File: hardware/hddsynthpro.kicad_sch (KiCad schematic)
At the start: 0 parts

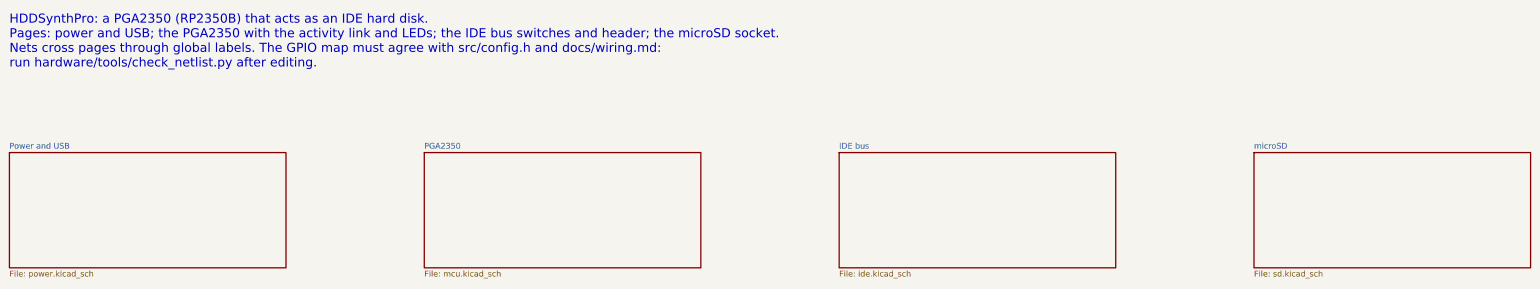
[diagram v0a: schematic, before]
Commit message: PCB rev 0.2: RP2350B on the board instead of the PGA2350 module
The PGA2350 is replaced by an RP2350B with Raspberry Pi's minimal-design
support circuit: their core regulator (polarity-marked inductor), 12 MHz
crystal, W25Q128 flash and USB 27R, with their regulator, QSPI and USB
layout copied relative to the VREG_LX pin; an AMS1117 makes 3V3. GPIO
numbers are unchanged. Supply pins each have a via under the chip.

Cheaper parts from the HDD Synth Mk5: HRO TYPE-C-31-M-12 USB-C, TS-1187A
buttons, and a generic TF PUSH microSD socket. The CB3T3245 bus switches
stay. Every symbol carries its LCSC part number, and Fabrication Toolkit
offsets where JLCPCB's footprint differs from KiCad's; jlcpcb.py applies
the same fitted corrections. check_netlist.py also checks the RP2350
support circuit. ERC and DRC are clean; parts for 5 boards about $68.50.

Co-Authored-By: Claude Opus 5.5 <noreply@anthropic.com>
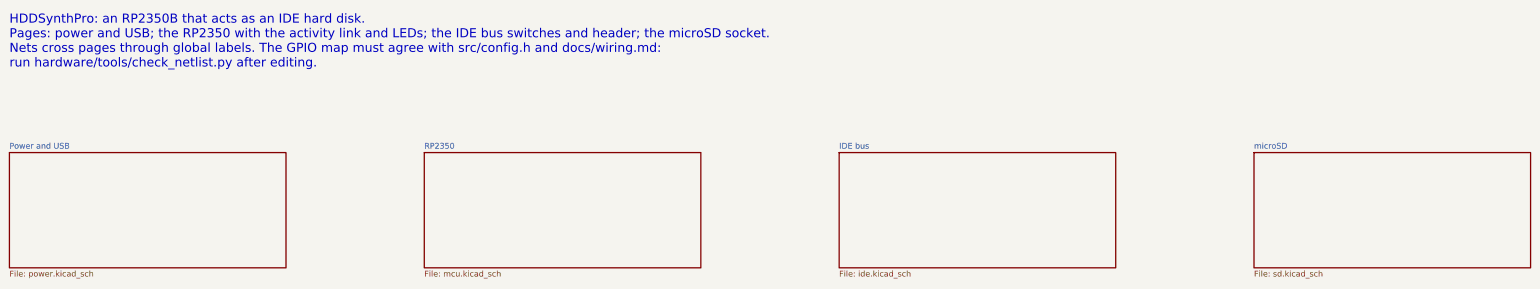
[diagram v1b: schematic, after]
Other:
- sheet PGA2350 renamed RP2350
- note added: "HDDSynthPro: an RP2350B that acts as an IDE hard disk. Pages: power and USB; the RP2350 with the activity link and LEDs; the IDE bus switches and header; the microSD socket. Nets cross pages through global labels. The GPIO map must agree with src/config.h and docs/wiring.md: run hardware/tools/check_netlist.py after editing."
- note removed: "HDDSynthPro: a PGA2350 (RP2350B) that acts as an IDE hard disk. Pages: power and USB; the PGA2350 with the activity link and LEDs; the IDE bus switches and header; the microSD socket. Nets cross pages through global labels. The GPIO map must agree with src/config.h and docs/wiring.md: run hardware/tools/check_netlist.py after editing."
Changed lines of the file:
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@@
 			(color 0 0 0 0)
 		)
-		(property "Sheetname" "PGA2350"
+		(property "Sheetname" "RP2350"
 			(at 121.92 60.2484 0)
 			(effects
@@
 		)
 	)
-	(text "HDDSynthPro: a PGA2350 (RP2350B) that acts as an IDE hard disk.\nPages: power and USB; the PGA2350 with the activity link and LEDs; the IDE bus switches and header; the microSD socket.\nNets cross pages through global labels. The GPIO map must agree with src/config.h and docs/wiring.md:\nrun hardware/tools/check_netlist.py after editing."
+	(text "HDDSynthPro: an RP2350B that acts as an IDE hard disk.\nPages: power and USB; the RP2350 with the activity link and LEDs; the IDE bus switches and header; the microSD socket.\nNets cross pages through global labels. The GPIO map must agree with src/config.h and docs/wiring.md:\nrun hardware/tools/check_netlist.py after editing."
 		(exclude_from_sim no)
 		(at 30.48 30.48 0)
